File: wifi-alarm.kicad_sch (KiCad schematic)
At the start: 1 part, among them J1 Screw_Terminal_01x02

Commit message: finished without LAN
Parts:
- added C12: 1u, Capacitor_SMD:C_0603_1608Metric_Pad1.08x0.95mm_HandSolder, symbol Device:C_Small
- added C13: 100n, Capacitor_SMD:C_0402_1005Metric_Pad0.74x0.62mm_HandSolder, symbol Device:C_Small
- added C15, C17: 22u, Capacitor_SMD:C_1206_3216Metric_Pad1.33x1.80mm_HandSolder, symbol Device:C_Small
- added C16: 100n, Capacitor_SMD:C_0603_1608Metric_Pad1.08x0.95mm_HandSolder, symbol Device:C_Small
- added D3, D5, D6, D7: ESD9B3.3ST5G, Diode_SMD:D_SOD-923, symbol Diode:ESD9B3.3ST5G
- added H1, H2, H3, H4: MountingHole, MountingHole:MountingHole_2.5mm_Pad, symbol Mechanical:MountingHole_Pad
- added J2: DM3AT-SF-PEJM5_40_, footprints:DM3ATSFPEJM540, symbol DM3AT-SF-PEJM5_40_:DM3AT-SF-PEJM5_40_
- added J3: Conn_ARM_JTAG_SWD_20, Connector_IDC:IDC-Header_2x10_P2.54mm_Vertical, symbol Connector:Conn_ARM_JTAG_SWD_20
- added Q1, Q2: MMBT2222A, Package_TO_SOT_SMD:SOT-23, symbol Transistor_BJT:MMBT2222A
- added R10, R11, R12, R13: 100, Resistor_SMD:R_0603_1608Metric_Pad0.98x0.95mm_HandSolder, symbol Device:R_Small
- added R15, R17: 10k, Resistor_SMD:R_0603_1608Metric_Pad0.98x0.95mm_HandSolder, symbol Device:R
- added R6, R7: 10K, Resistor_SMD:R_0603_1608Metric_Pad0.98x0.95mm_HandSolder, symbol Device:R_Small
- added R9: 1k, Resistor_SMD:R_0603_1608Metric_Pad0.98x0.95mm_HandSolder, symbol Device:R
- added S1: FSM4JSMATR, digikey-footprints:Switch_Tactile_SMD_6x6mm, symbol dk_Tactile-Switches:FSM4JSMATR
- added TP1, TP19, TP2, TP20, TP21, TP22, TP23, TP24, TP25, TP26, TP27, TP28, TP29, TP3, TP30, TP31, TP32, TP33, TP34: (no value), TestPoint:TestPoint_Pad_1.5x1.5mm, symbol Connector:TestPoint_Small
- added U2: ESP32-S3-WROOM-1, RF_Module:ESP32-S3-WROOM-1, symbol RF_Module:ESP32-S3-WROOM-1
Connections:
- net 3.3V_OUT: now also C13.1, C15.1, C16.1, C17.1, J2.4 (VDD), R6.1, R7.1, R9.1, TP2.1, U2.2 (3V3)
- net 5V_OUT: now also TP1.1
- net GND: now also C12.2, C13.2, C15.2, C16.2, C17.2, D3.1 (A1), D5.1 (A1), D6.1 (A1), D7.1 (A1), H1.1, H2.1, H3.1, H4.1, J2.6 (VSS), J3.10 (GND), J3.12 (GND), J3.14 (GND), J3.16 (GND), J3.18 (GND), J3.20 (GND), J3.4 (GND), J3.6 (GND), J3.8 (GND), S1.2, TP32.1, U2.1 (GND), U2.40 (GND), U2.41 (GND)
- net PWR_INPUT: now also TP3.1
- new net: R12.2, U2.22 (IO14)
- new net: R13.2, U2.8 (IO15)
- new net: Q1.1 (B), R15.2
- new net: R10.2, U2.20 (IO12)
- new net: R11.2, U2.21 (IO13)
- new net: Q2.1 (B), R17.2
- new net CP_DTR: Q1.2 (E), R17.1, TP27.1
- new net CP_RTS: Q2.2 (E), R15.1, TP26.1
- new net EN: C12.1, Q2.3 (C), R7.2, S1.3, TP33.1, U2.3 (EN)
- new net IO0: Q1.3 (C), R6.2, TP34.1, U2.27 (IO0)
- new net RL_1: U2.15 (IO3)
- new net RL_2: U2.4 (IO4)
- new net RL_3: U2.5 (IO5)
- new net Rx: TP24.1, U2.37 (TXD0)
- new net SD_CLK: J2.5 (CLK), TP21.1, U2.13 (IO19)
- new net SD_CS: J2.2 (CD/DAT3), R9.2, TP23.1, U2.14 (IO20)
- new net SD_DETECT: J2.CD1 (CARD_DETECT), TP22.1, U2.23 (IO21)
- new net SD_MISO: J2.7 (DAT0), TP20.1, U2.11 (IO18)
- new net SD_MOSI: J2.3 (CMD), TP19.1, U2.10 (IO17)
- new net TCK: D7.2 (A2), J3.9 (TCK/SWCLK), R11.1, TP31.1
- new net TDI: D3.2 (A2), J3.5 (TDI), R10.1, TP28.1
- new net TDO: D5.2 (A2), J3.13 (TDO/SWO), R13.1, TP29.1
- new net TMS: D6.2 (A2), J3.7 (TMS/SWDIO), R12.1, TP30.1
- new net TR_1: U2.6 (IO6)
- new net TR_2: U2.7 (IO7)
- new net Tx: TP25.1, U2.36 (RXD0)
- no-connect marks 0 -> 33
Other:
- added sheet outputs (outputs.kicad_sch)
- added sheet usb_prog (usb_prog.kicad_sch)
- note added: "OUTPUT CIRCUIT"
- note added: "POWER CIRCUIT"
- note added: "SDCARD CIRCUIT"
- note added: "USB CIRCUIT"
- moved on the sheet: J1

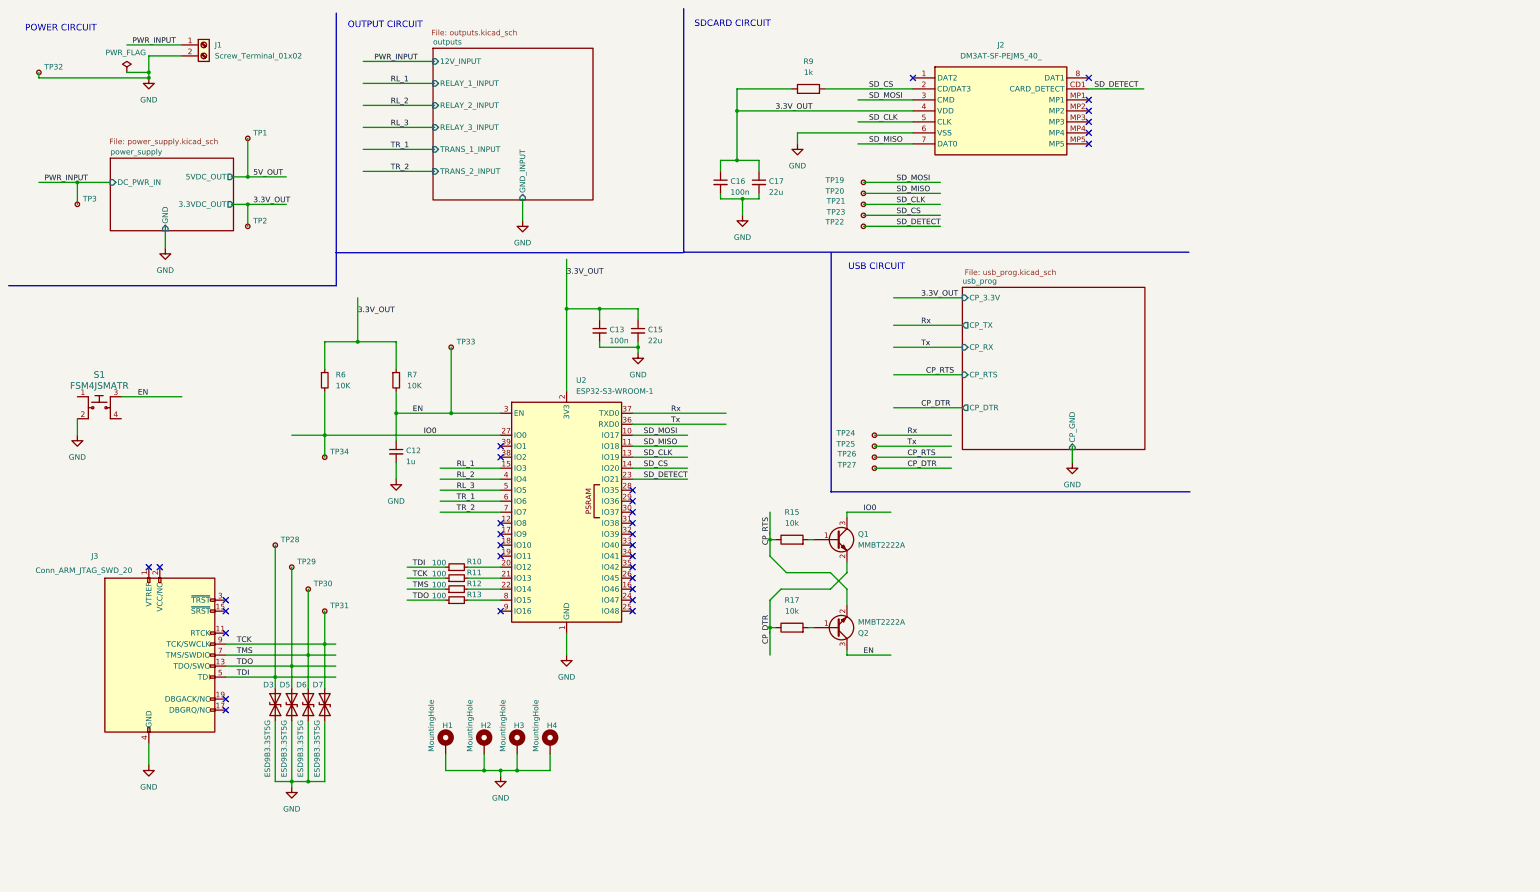
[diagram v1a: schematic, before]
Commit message: Correct pins in schematics and add LAN8270
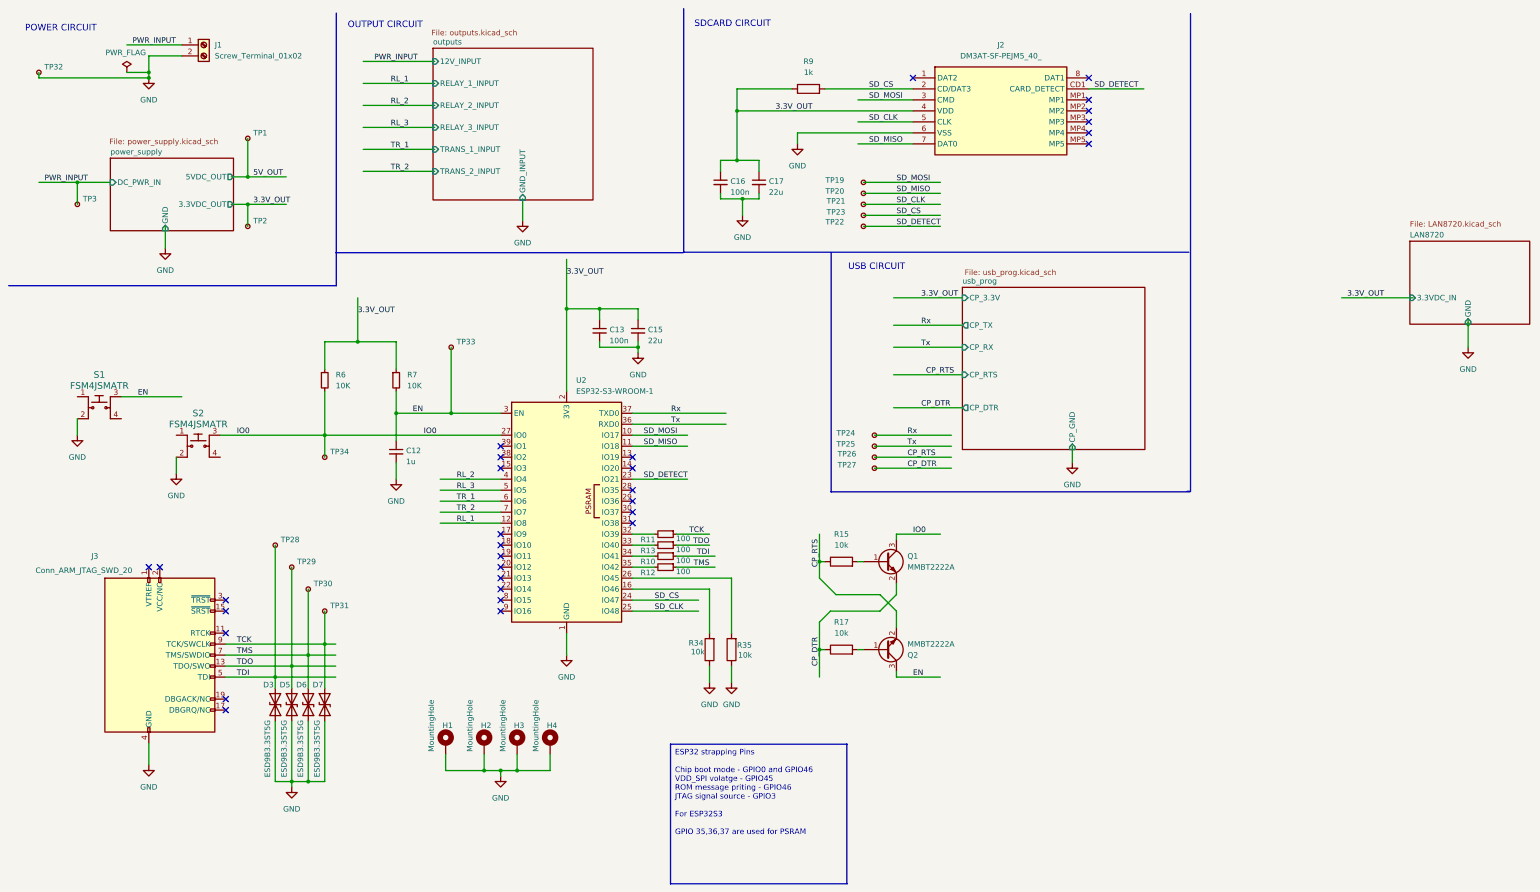
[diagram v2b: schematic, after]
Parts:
- added R34, R35: 10k, Resistor_SMD:R_0603_1608Metric_Pad0.98x0.95mm_HandSolder, symbol Device:R
- added S2: FSM4JSMATR, digikey-footprints:Switch_Tactile_SMD_6x6mm, symbol dk_Tactile-Switches:FSM4JSMATR
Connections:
- net GND: now also R34.1, R35.1, S2.2
- net IO0: now also S2.3
- net RL_1: now also U2.12 (IO8); no longer U2.15 (IO3)
- net SD_CLK: now also U2.25 (IO48); no longer U2.13 (IO19)
- net SD_CS: now also U2.24 (IO47); no longer U2.14 (IO20)
- net at U2.22 (IO14): no longer R12.2
- net at R13.2: now also U2.33 (IO40); no longer U2.8 (IO15)
- net at U2.16 (IO46): now also R34.2
- net at U2.20 (IO12): no longer R10.2
- net at U2.21 (IO13): no longer R11.2
- net at U2.26 (IO45): now also R35.2
- net at U2.32 (IO39): now also R11.2
- net at U2.34 (IO41): now also R10.2
- net at U2.35 (IO42): now also R12.2
- no-connect marks 33 -> 31
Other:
- added sheet LAN8720 (LAN8720.kicad_sch)
- moved on the sheet: Q1, Q2, R15, R17

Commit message: Add w5500 LAN to SPI because S3 does not have RMII, so we can't use LAN8720
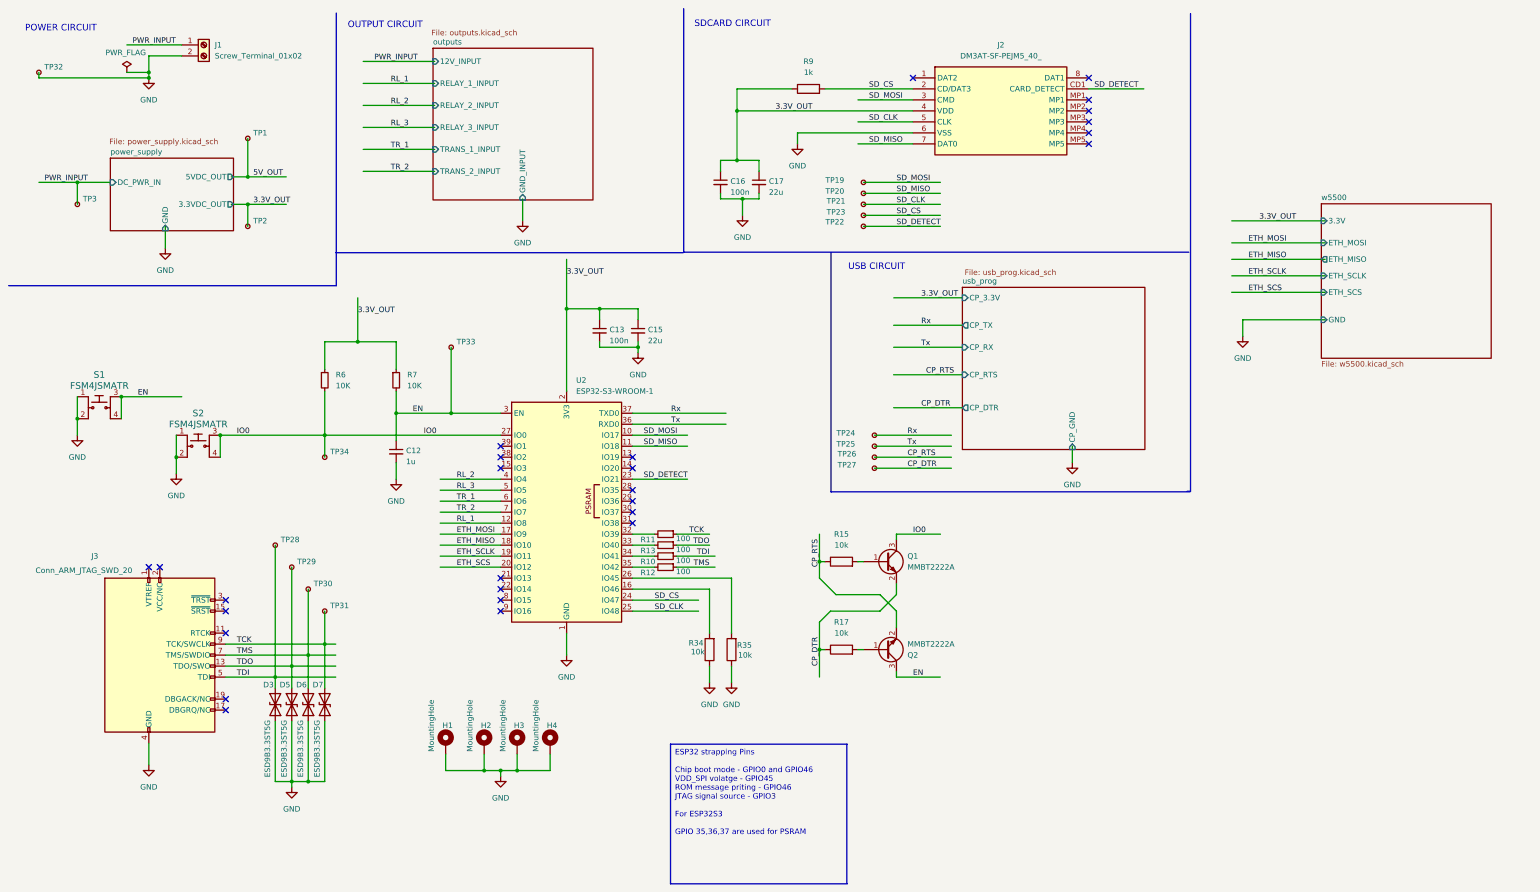
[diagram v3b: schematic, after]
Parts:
- C13: footprint Capacitor_SMD:C_0402_1005Metric_Pad0.74x0.62mm_HandSolder -> Capacitor_SMD:C_0603_1608Metric_Pad1.08x0.95mm_HandSolder
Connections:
- net EN: now also S1.4
- net GND: now also S1.1, S2.1
- net IO0: now also S2.4
- net ETH_MOSI: now reaches U2.17 (IO9)
- net ETH_MISO: now reaches U2.18 (IO10)
- net ETH_SCLK: now reaches U2.19 (IO11)
- net ETH_SCS: now reaches U2.20 (IO12)
- no-connect marks 31 -> 27
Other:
- removed sheet LAN8720
- added sheet w5500 (w5500.kicad_sch)
